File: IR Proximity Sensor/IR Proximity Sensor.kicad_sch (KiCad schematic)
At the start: 9 parts, among them J1 Power & O/P Pins, U1 LM358

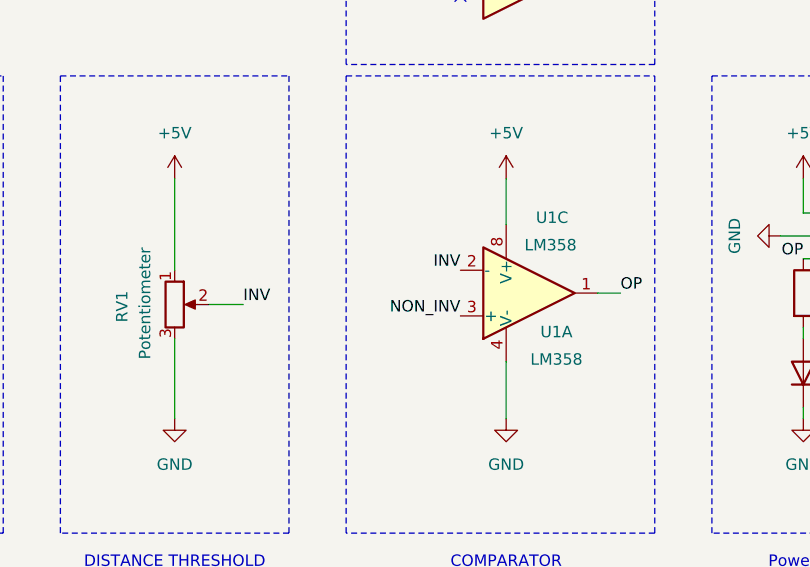
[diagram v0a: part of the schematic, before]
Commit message: Done with PCB routing and zone filling
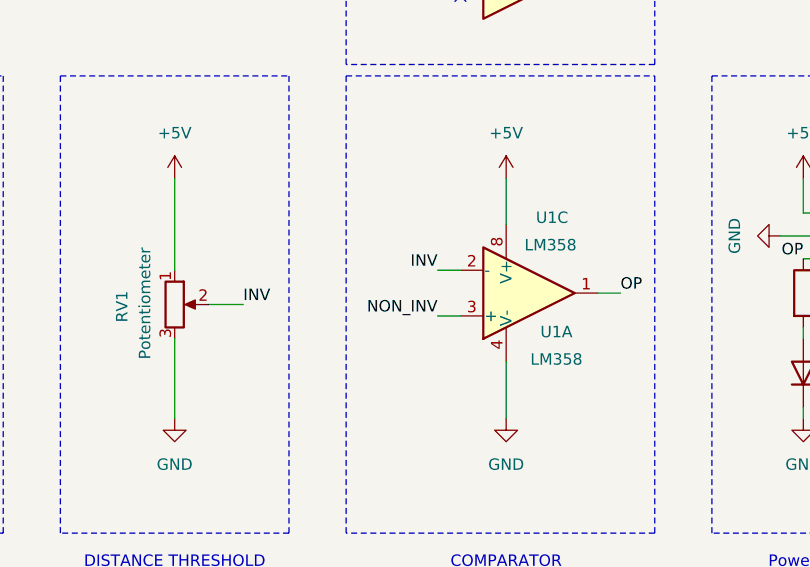
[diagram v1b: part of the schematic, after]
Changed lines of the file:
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@@
+	(wire
+		(pts
+			(xy 173.99 92.71) (xy 176.53 92.71)
+		)
+		(stroke
+			(width 0)
+			(type default)
+		)
+	)
 	(wire
 		(pts
@@
 		(pts
 			(xy 113.03 105.41) (xy 113.03 109.22)
+		)
+		(stroke
+			(width 0)
+			(type default)
+		)
+	)
+	(wire
+		(pts
+			(xy 173.99 97.79) (xy 176.53 97.79)
 		)
 		(stroke
@@
 	)
 	(label "INV"
-		(at 176.53 92.71 180)
+		(at 173.99 92.71 180)
 		(effects
 			(font
@@
 	)
 	(label "NON_INV"
-		(at 176.53 97.79 180)
+		(at 173.99 97.79 180)
 		(effects
 			(font

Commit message: Updated footprints and PCB layout
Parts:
- removed J1: Power & O/P Pins, Connector_PinSocket_2.54mm:PinSocket_1x03_P2.54mm_Horizontal, symbol Connector_Generic:Conn_01x03
- added J1: Conn_01x03_Pin, Connector_PinHeader_2.54mm:PinHeader_1x03_P2.54mm_Horizontal, symbol Connector:Conn_01x03_Pin
- D1: footprint LED_THT:LED_D3.0mm_IRBlack -> LED_THT:LED_D3.0mm_Horizontal_O3.81mm_Z2.0mm
- D2: footprint LED_THT:LED_D3.0mm -> LED_THT:LED_D3.0mm_Horizontal_O3.81mm_Z2.0mm
- D3: footprint LED_THT:LED_D3.0mm -> LED_SMD:LED_1206_3216Metric
- R1, R2, R3: footprint Resistor_THT:R_Axial_DIN0207_L6.3mm_D2.5mm_P7.62mm_Horizontal -> Resistor_SMD:R_1206_3216Metric
- RV1: footprint Potentiometer_SMD:Potentiometer_ACP_CA6-VSMD_Vertical -> Potentiometer:TRIM_3362P-1-103
- U1: footprint Package_DIP:DIP-8_W7.62mm -> Package_SO:TSSOP-8_3x3mm_P0.65mm
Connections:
- net +5V: now also J1.1 (Pin_1)
- net GND: now also J1.2 (Pin_2)
- net OP: now also J1.3 (Pin_3)
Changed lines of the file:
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@@
 			)
 		)
-		(property "Footprint" "Resistor_THT:R_Axial_DIN0207_L6.3mm_D2.5mm_P7.62mm_Horizontal"
+		(property "Footprint" "Resistor_SMD:R_1206_3216Metric"
 			(at 212.852 95.25 90)
 			(effects
@@
 	)
 	(symbol
-		(lib_id "Connector_Generic:Conn_01x03")
-		(at 220.98 88.9 0)
-		(unit 1)
-		(exclude_from_sim no)
-		(in_bom yes)
-		(on_board yes)
-		(dnp no)
-		(property "Reference" "J1"
-			(at 224.536 89.408 90)
-			(effects
-				(font
-					(size 1.27 1.27)
-				)
-				(justify left)
-			)
-		)
-		(property "Value" "Power & O/P Pins"
-			(at 227.076 96.52 90)
-			(effects
-				(font
-					(size 1.27 1.27)
-				)
-				(justify left)
-			)
-		)
-		(property "Footprint" "Connector_PinSocket_2.54mm:PinSocket_1x03_P2.54mm_Horizontal"
-			(at 220.98 88.9 0)
-			(effects
-				(font
-					(size 1.27 1.27)
-				)
-				(hide yes)
-			)
-		)
-		(property "Datasheet" "~"
-			(at 220.98 88.9 0)
-			(effects
-				(font
-					(size 1.27 1.27)
-				)
-				(hide yes)
-			)
-		)
-		(property "Description" "Generic connector, single row, 01x03, script generated (kicad-library-utils/schlib/autogen/connector/)"
-			(at 220.98 88.9 0)
-			(effects
-				(font
-					(size 1.27 1.27)
-				)
-				(hide yes)
-			)
-		)
-		(pin "1"
-		)
-		(pin "2"
-		)
-		(pin "3"
-		)
-		(instances
-			(project ""
-				(path "/5db8d884-e15d-42ac-b10d-9d70dbe2c29e"
-					(reference "J1")
-					(unit 1)
-				)
-			)
-		)
-	)
-	(symbol
 		(lib_id "Device:D_Photo")
 		(at 113.03 91.44 270)
@@
 			)
 		)
-		(property "Footprint" "LED_THT:LED_D3.0mm"
+		(property "Footprint" "LED_THT:LED_D3.0mm_Horizontal_O3.81mm_Z2.0mm"
 			(at 113.03 90.17 0)
 			(effects
@@
 			)
 		)
-		(property "Footprint" "LED_THT:LED_D3.0mm_IRBlack"
+		(property "Footprint" "LED_THT:LED_D3.0mm_Horizontal_O3.81mm_Z2.0mm"
 			(at 76.835 88.9 0)
 			(effects
@@
 			)
 		)
-		(property "Footprint" "Resistor_THT:R_Axial_DIN0207_L6.3mm_D2.5mm_P7.62mm_Horizontal"
+		(property "Footprint" "Resistor_SMD:R_1206_3216Metric"
 			(at 111.252 101.6 90)
 			(effects
@@
 			)
 		)
-		(property "Footprint" "Package_DIP:DIP-8_W7.62mm"
+		(property "Footprint" "Package_SO:TSSOP-8_3x3mm_P0.65mm"
 			(at 184.15 59.69 0)
 			(effects
@@
 			)
 		)
-		(property "Footprint" "Resistor_THT:R_Axial_DIN0207_L6.3mm_D2.5mm_P7.62mm_Horizontal"
+		(property "Footprint" "Resistor_SMD:R_1206_3216Metric"
 			(at 79.502 101.6 90)
 			(effects
@@
 			)
 		)
-		(property "Footprint" "Package_DIP:DIP-8_W7.62mm"
+		(property "Footprint" "Package_SO:TSSOP-8_3x3mm_P0.65mm"
 			(at 184.15 95.25 0)
 			(effects
@@
 	)
 	(symbol
+		(lib_id "Connector:Conn_01x03_Pin")
+		(at 220.98 88.9 0)
+		(mirror y)
+		(unit 1)
+		(exclude_from_sim no)
+		(in_bom yes)
+		(on_board yes)
+		(dnp no)
+		(property "Reference" "J1"
+			(at 220.345 81.28 0)
+			(effects
+				(font
+					(size 1.27 1.27)
+				)
+			)
+		)
+		(property "Value" "Conn_01x03_Pin"
+			(at 220.345 83.82 0)
+			(effects
+				(font
+					(size 1.27 1.27)
+				)
+			)
+		)
+		(property "Footprint" "Connector_PinHeader_2.54mm:PinHeader_1x03_P2.54mm_Horizontal"
+			(at 220.98 88.9 0)
+			(effects
+				(font
+					(size 1.27 1.27)
+				)
+				(hide yes)
+			)
+		)
+		(property "Datasheet" "~"
+			(at 220.98 88.9 0)
+			(effects
+				(font
+					(size 1.27 1.27)
+				)
+				(hide yes)
+			)
+		)
+		(property "Description" "Generic connector, single row, 01x03, script generated"
+			(at 220.98 88.9 0)
+			(effects
+				(font
+					(size 1.27 1.27)
+				)
+				(hide yes)
+			)
+		)
+		(pin "2"
+		)
+		(pin "3"
+		)
+		(pin "1"
+		)
+		(instances
+			(project ""
+				(path "/5db8d884-e15d-42ac-b10d-9d70dbe2c29e"
+					(reference "J1")
+					(unit 1)
+				)
+			)
+		)
+	)
+	(symbol
 		(lib_id "Device:LED")
 		(at 214.63 104.14 90)
@@
 			)
 		)
-		(property "Footprint" "LED_THT:LED_D3.0mm"
+		(property "Footprint" "LED_SMD:LED_1206_3216Metric"
 			(at 214.63 104.14 0)
 			(effects
@@
 			)
 		)
-		(property "Footprint" "Package_DIP:DIP-8_W7.62mm"
+		(property "Footprint" "Package_SO:TSSOP-8_3x3mm_P0.65mm"
 			(at 184.15 95.25 0)
 			(effects
@@
 			)
 		)
-		(property "Footprint" "Potentiometer_SMD:Potentiometer_ACP_CA6-VSMD_Vertical"
+		(property "Footprint" "Potentiometer:TRIM_3362P-1-103"
 			(at 144.78 96.52 0)
 			(effects
